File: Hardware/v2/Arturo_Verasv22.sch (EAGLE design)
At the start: 23 parts, among them T1 2SC1815, T3 2SC1815, T4 2SC1815, T5 2SC1815, T6 2SC1815, T7 2SC1815, T8 2SC1815, X1 22-23-2071

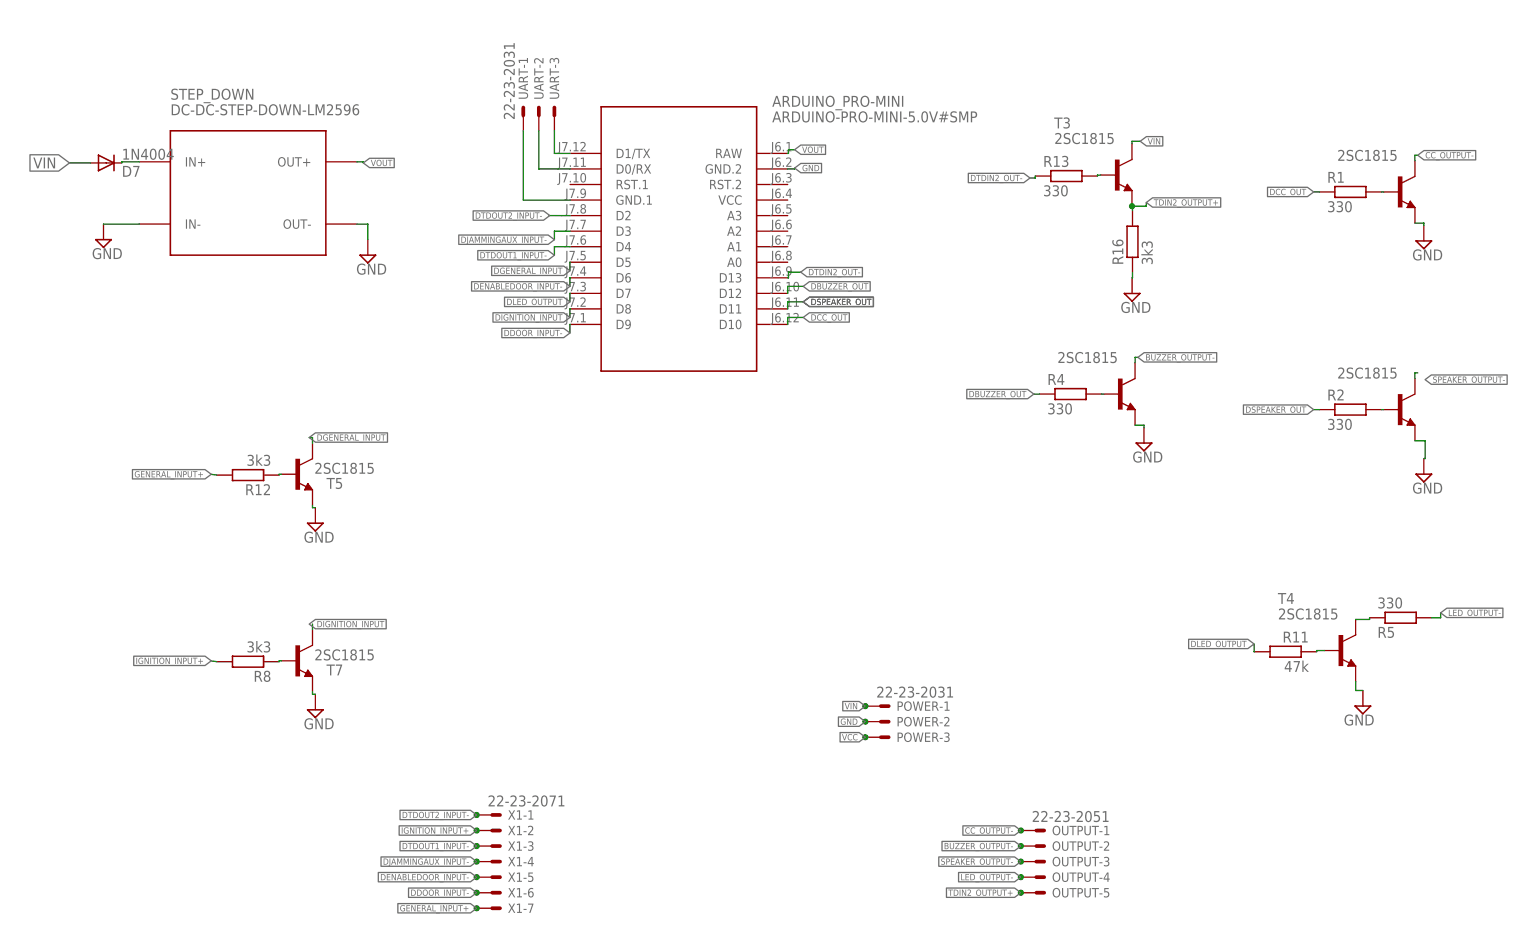
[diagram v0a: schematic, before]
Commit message: Esquematico
se hace más simple el esquemático
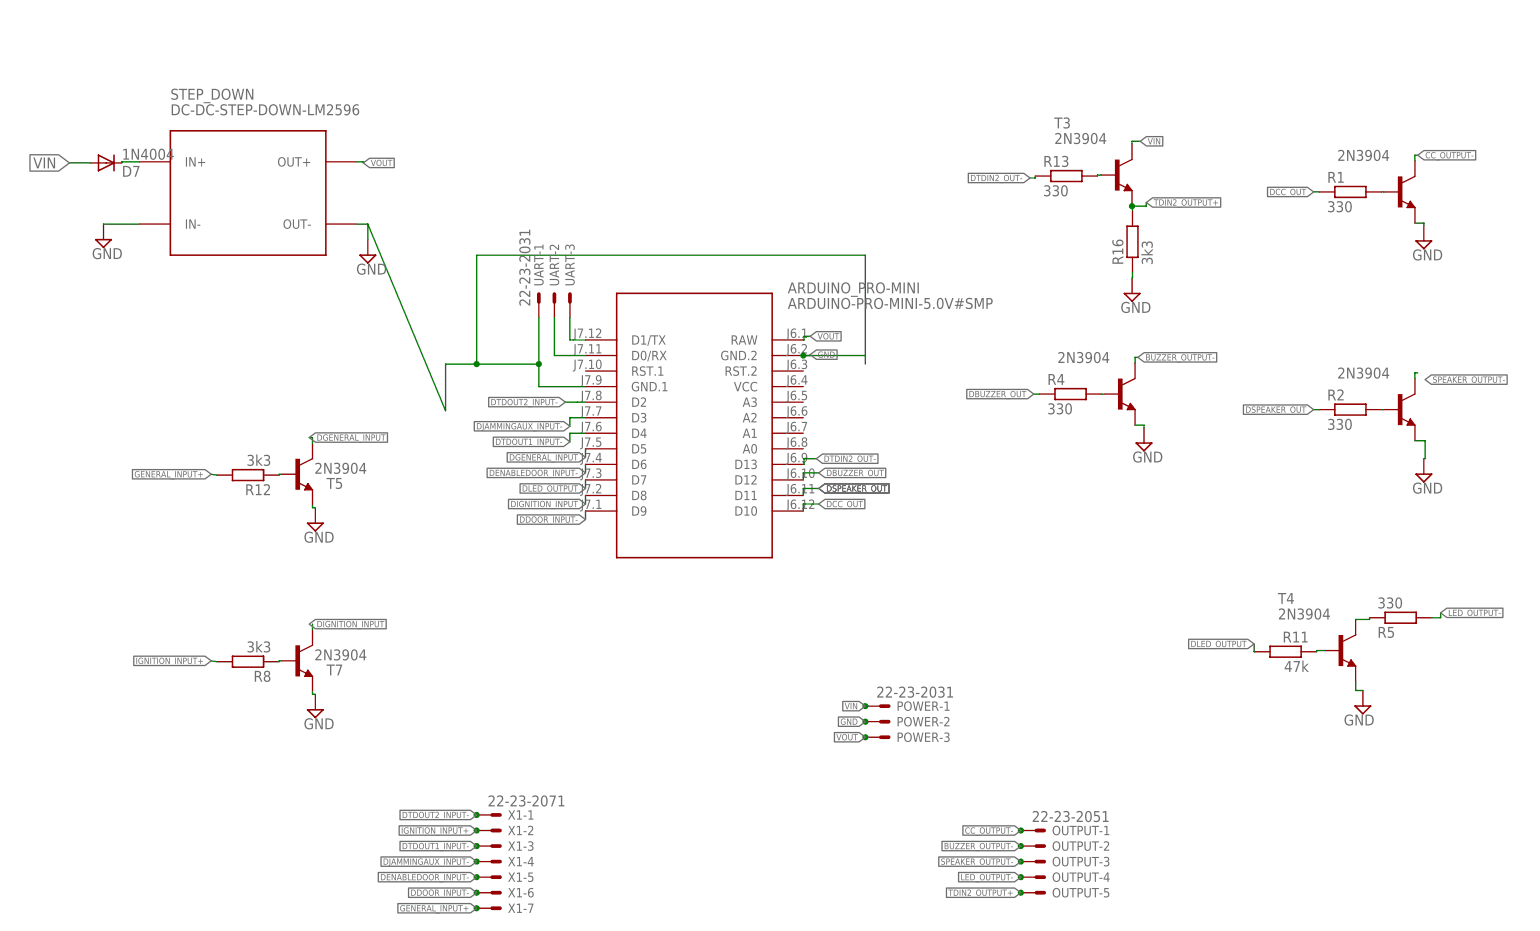
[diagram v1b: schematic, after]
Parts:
- T1, T3, T4, T5, T6, T7, T8: value 2SC1815 -> 2N3904; device transistor:2SC1815 -> transistor:2N3904
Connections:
- removed net N$9: ARDUINO_PRO-MINI.GND.1, UART-1.S
- removed net VCC: POWER-3.S
- net GND: now also ARDUINO_PRO-MINI.GND.1, UART-1.S
- net VOUT: now also POWER-3.S
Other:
- moved on the sheet: ARDUINO_PRO-MINI, UART-1, UART-2, UART-3
